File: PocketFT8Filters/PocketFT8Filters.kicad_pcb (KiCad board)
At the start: 2 copper layers, 38.1 x 12.7 mm, 8 parts

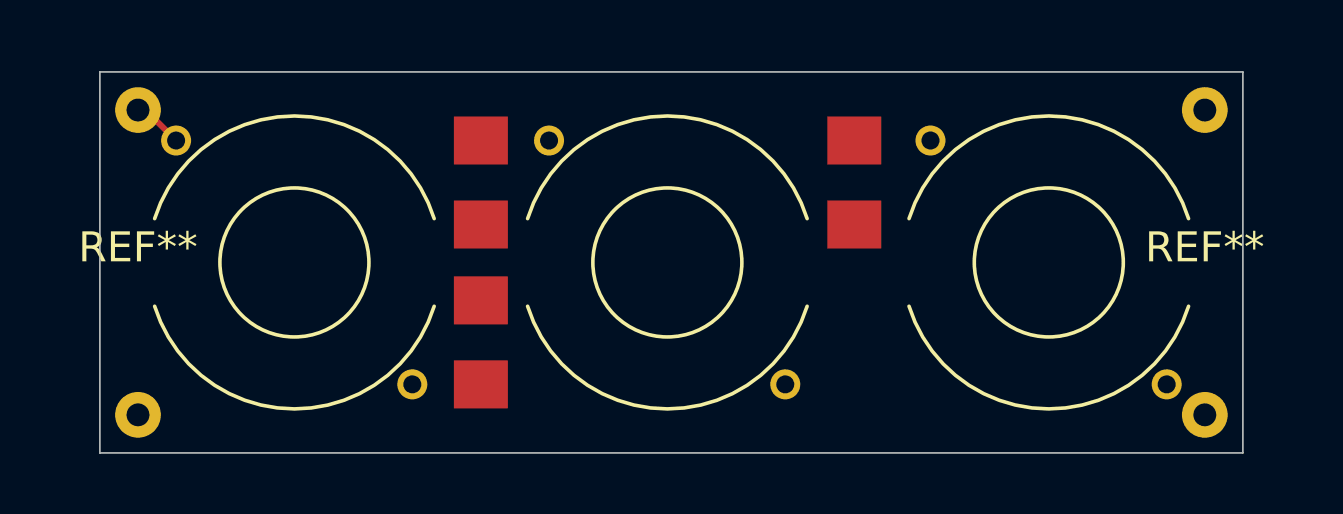
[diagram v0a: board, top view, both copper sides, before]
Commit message: Both the main board and filter board submitted to PCBway
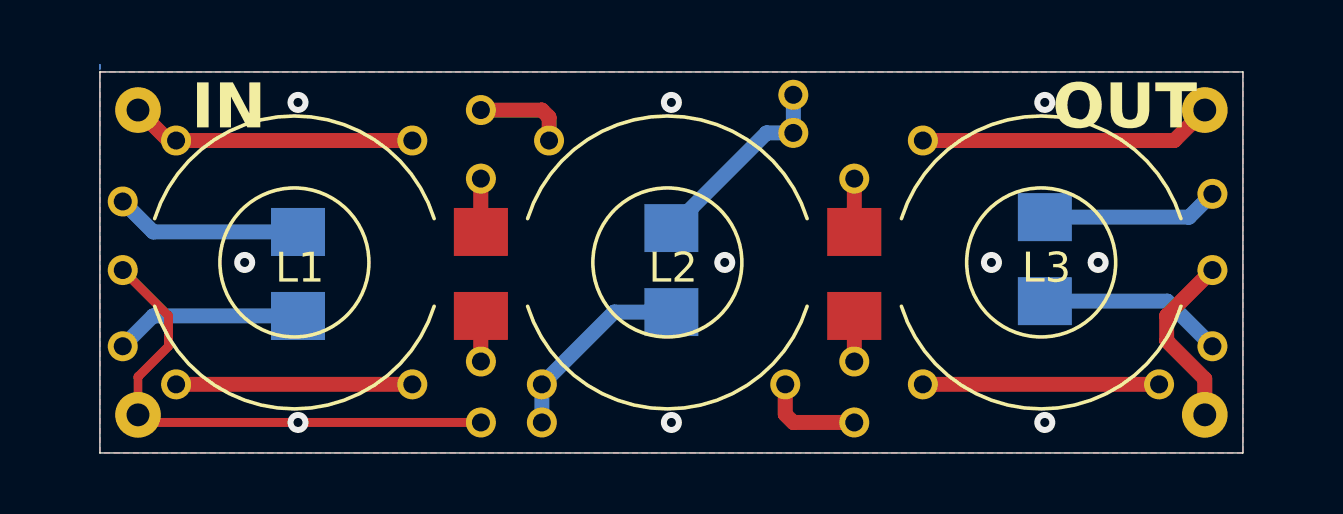
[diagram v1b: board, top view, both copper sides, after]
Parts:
- added REF**: THTPAD, Filters:THTPAD, F.Cu at (86.6, 78.5)
- added REF**: THTPAD, Filters:THTPAD, F.Cu at (103.6, 86.6)
- added REF**: THTPAD, Filters:THTPAD, F.Cu at (88.9, 79.8)
- added REF**: THTPAD, Filters:THTPAD, F.Cu at (88.9, 77.5)
- added REF**: THTPAD, Filters:THTPAD, F.Cu at (99.3, 78.2)
- added REF**: THTPAD, Filters:THTPAD, F.Cu at (113.3, 85.3)
- added REF**: THTPAD, Filters:THTPAD, F.Cu at (77.0, 82.8)
- added REF**: THTPAD, Filters:THTPAD, F.Cu at (77.0, 85.3)
- added REF**: THTPAD, Filters:THTPAD, F.Cu at (77.0, 80.5)
- added REF**: THTPAD, Filters:THTPAD, F.Cu at (101.3, 85.9)
- added REF**: THTPAD, Filters:THTPAD, F.Cu at (86.6, 86.6)
- added REF**: THTPAD, Filters:THTPAD, F.Cu at (113.3, 82.8)
- added REF**: THTPAD, Filters:THTPAD, F.Cu at (101.3, 87.9)
- added REF**: THTPAD, Filters:THTPAD, F.Cu at (99.3, 77.0)
- added REF**: THTPAD, Filters:THTPAD, F.Cu at (88.9, 87.9)
- added REF**: THTPAD, Filters:THTPAD, F.Cu at (101.3, 79.8)
- added REF**: 1206, SparkFun-Fuse:1206, B.Cu at (95.2, 82.8)
- added REF**: 1206, SparkFun-Fuse:1206, B.Cu at (107.7, 82.4)
- added REF**: THTPAD, Filters:THTPAD, F.Cu at (90.9, 87.9)
- added REF**: THTPAD, Filters:THTPAD, F.Cu at (90.9, 86.6)
- added REF**: THTPAD, Filters:THTPAD, F.Cu at (113.3, 80.3)
- added REF**: THTPAD, Filters:THTPAD, F.Cu at (88.9, 85.9)
- REF**: moved to B.Cu
- moved REF** 6.51 mm to (82.8, 82.9)
- moved REF** 3.05 mm to (88.9, 82.9)
- moved REF** 3.05 mm to (101.3, 82.9)
- moved REF** 0.25 mm to (100.1, 82.5)
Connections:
- REF** pad 1: (no net) -> C2-1
- REF** pad 2: (no net) -> C2-2
- REF** pad 1: (no net) -> L2-1
- REF** pad 2: (no net) -> L2-2
- REF** pad 1: (no net) -> OUT
- REF** pad 2: (no net) -> L3-2
- REF** pad 1: (no net) -> C4-1
- REF** pad 2: (no net) -> C4-2
- REF** pad 1: (no net) -> C1-1
- REF** pad 2: (no net) -> C1-2
- REF** pad 3: (no net) -> OUT
- REF** pad 4: (no net) -> GND
- REF** pad 1: (no net) -> IN (x2)
- REF** pad 2: (no net) -> GND
- REF** pad 2: (no net) -> L1-2
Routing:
- net GND: track 0.00 -> 23.9 mm, vias 0 -> 10
- net OUT: track 0.00 -> 9.82 mm
- net IN: track 0.00 -> 9.56 mm
- net L1-2: track 0.00 -> 7.87 mm
- net L3-2: track 0.00 -> 7.87 mm
- net C3-1: track 0.00 -> 6.65 mm
- net C3-2: track 0.00 -> 6.59 mm
- net C1-1: track 0.00 -> 6.26 mm
- net C1-2: track 0.00 -> 6.26 mm
- net C5-2: track 0.00 -> 6.21 mm
- net C5-1: track 0.00 -> 5.91 mm
- net L2-2: track 0.00 -> 3.41 mm
- net L2-1: track 0.00 -> 3.15 mm
- net C4-1: track 0.00 -> 1.78 mm
- net C2-1: track 0.00 -> 1.78 mm
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- added copper zone on B.Cu, net GND
- added copper zone on F.Cu, net GND
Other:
- board text added: "C1"
- board text added: "C3"
- board text added: "C5"
- board text added: "IN"
- board text added: "L1"
- board text added: "L2"
- board text added: "L3"
- board text added: "OUT"
